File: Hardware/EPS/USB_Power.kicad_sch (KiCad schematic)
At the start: 7 parts, among them J401 USB_C_Receptacle_PowerOnly_6P, U401 NCP176AMX330TCG

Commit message: Finished EPS - v0.1.0
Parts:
- removed U401: NCP176AMX330TCG, NCP176AMX330TCG:NCP176AMX330TCG, symbol NCP176AMX330TCG:NCP176AMX330TCG
- added U401: AP7361C-33Y5-13, AP7361C-25Y5-13:AP7361C25Y513, symbol AP7361C-25Y5-13:AP7361C-25Y5-13
- C401, C402: value 1uF -> 4.7uF
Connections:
- net +3.3V: now also U401.5 (OUT)
- net GND: now also C401.2, U401.2 (GND_1), U401.6 (GND_2); no longer C401.1
- net USB_VBUS: now also C401.1, U401.1 (EN), U401.4 (IN); no longer C401.2
- no-connect marks 1 -> 2

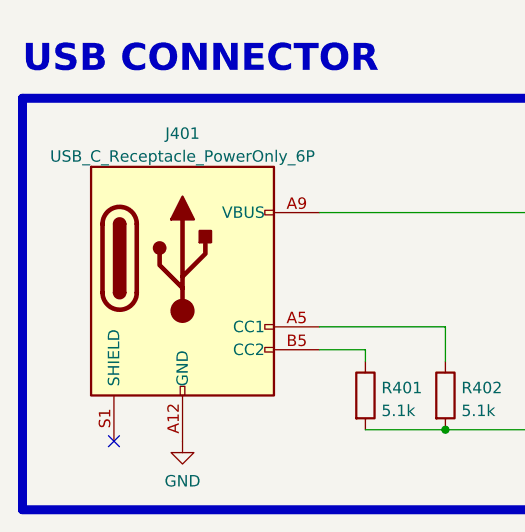
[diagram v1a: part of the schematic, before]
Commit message: Updated to KiCAD 7.0
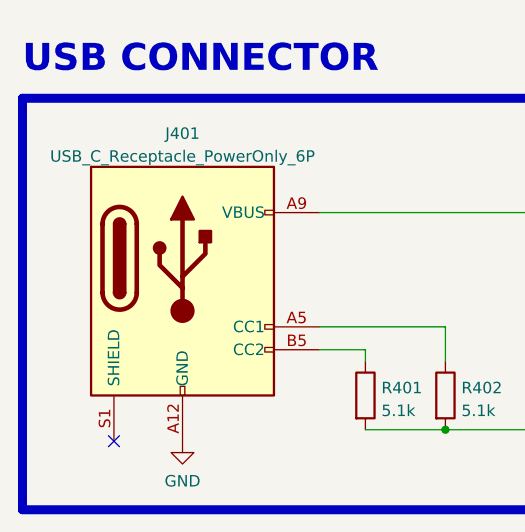
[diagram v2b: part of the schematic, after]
